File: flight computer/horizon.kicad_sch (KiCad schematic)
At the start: 38 parts, among them J2 Conn_02x03_Counter_Clockwise, J7 Conn_02x03_Counter_Clockwise, J8 Conn_02x03_Counter_Clockwise, SW1 CK_KMS2xxG, U1 MMCU, U2 MKL02Z32VFG4, U3 NMCU, U4 TMCU, Y1 Crystal

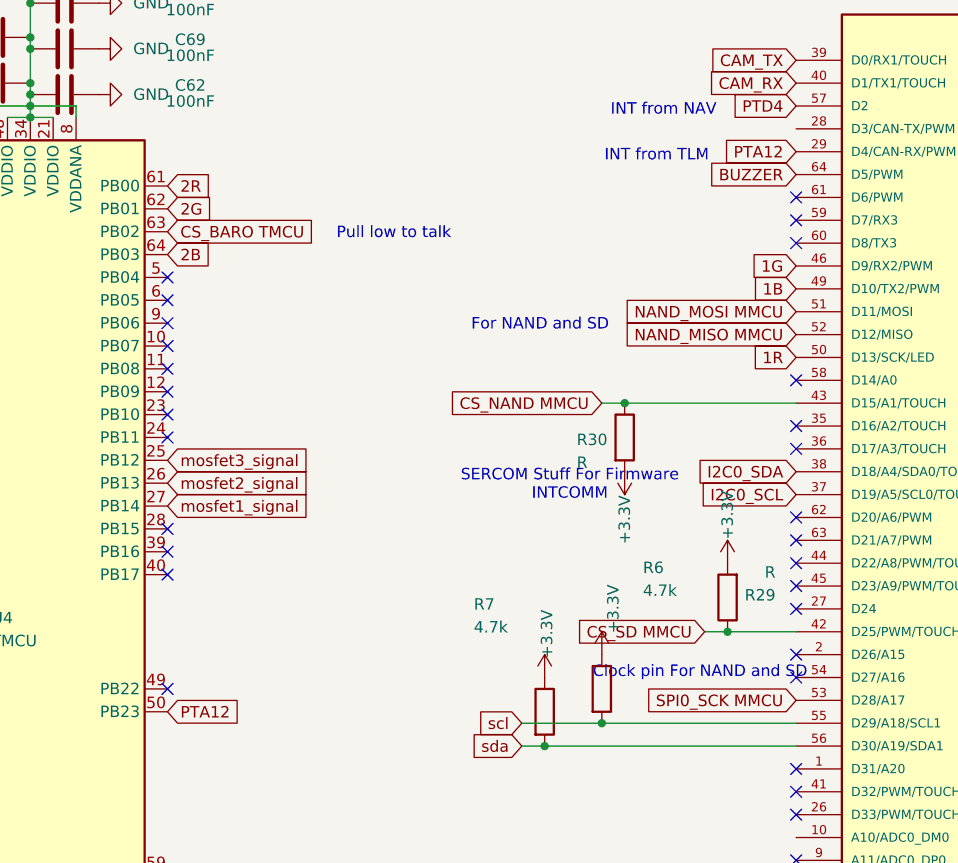
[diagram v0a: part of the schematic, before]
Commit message: one more trace besides for power...
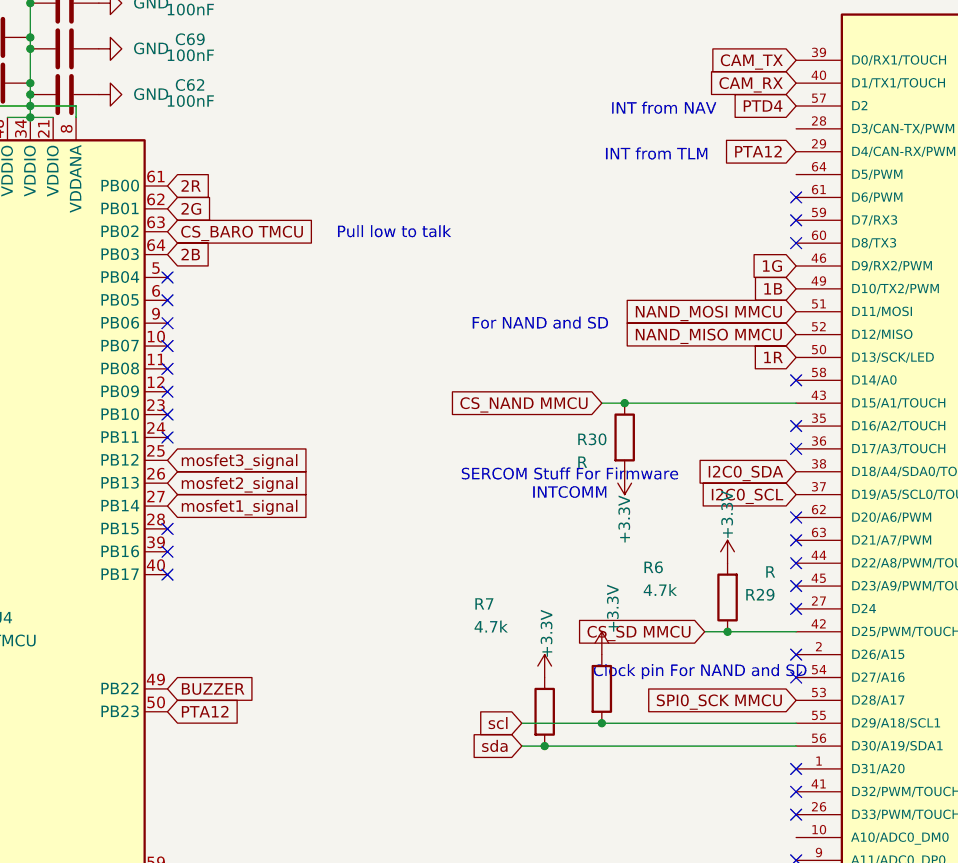
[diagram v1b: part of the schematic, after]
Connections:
- net BUZZER: now also U4.49 (PB22); no longer U1.64 (D5/PWM)
- no-connect marks 73 -> 72

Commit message: status light
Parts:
- added D18: SMLVN6RGB, LED_SMD:LED_ROHM_SMLVN6, symbol LED:SMLVN6RGB
- added R96, R97, R98: 220, Resistor_SMD:R_0603_1608Metric, symbol Device:R
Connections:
- net GND: now also D18.4 (GK), D18.5 (RK), D18.6 (BK)
- net StatusLED_2: now reaches U1.2 (D26/A15)
- net StatusLED_2: now also R97.1
- net StatusLED_1: now reaches U1.27 (D24)
- net StatusLED_1: now also R98.1
- net StatusLED_3: now reaches U1.41 (D32/PWM/TOUCH)
- net StatusLED_3: now also R96.1
- new net: D18.2 (RA), R97.2
- new net: D18.3 (GA), R96.2
- new net: D18.1 (BA), R98.2
- no-connect marks 72 -> 69

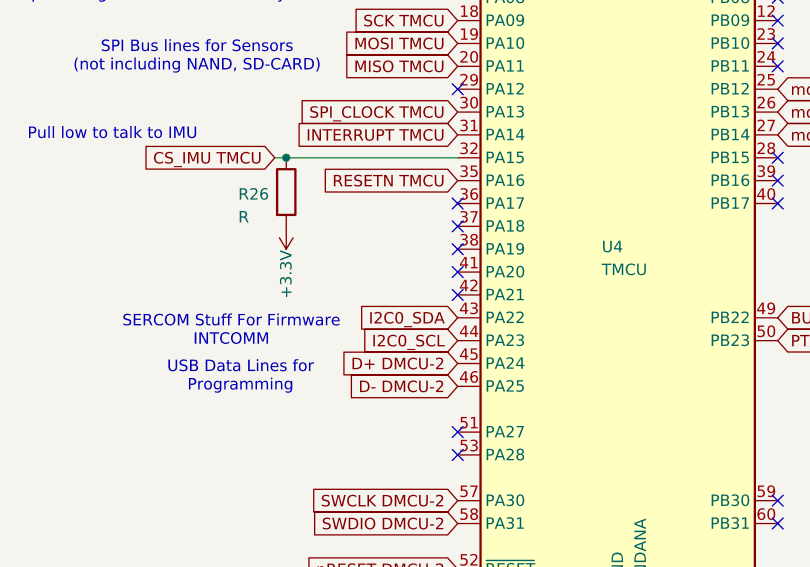
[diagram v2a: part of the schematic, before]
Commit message: Meddy, the PCB is ready for you. The proper RF is setup too on the PCB
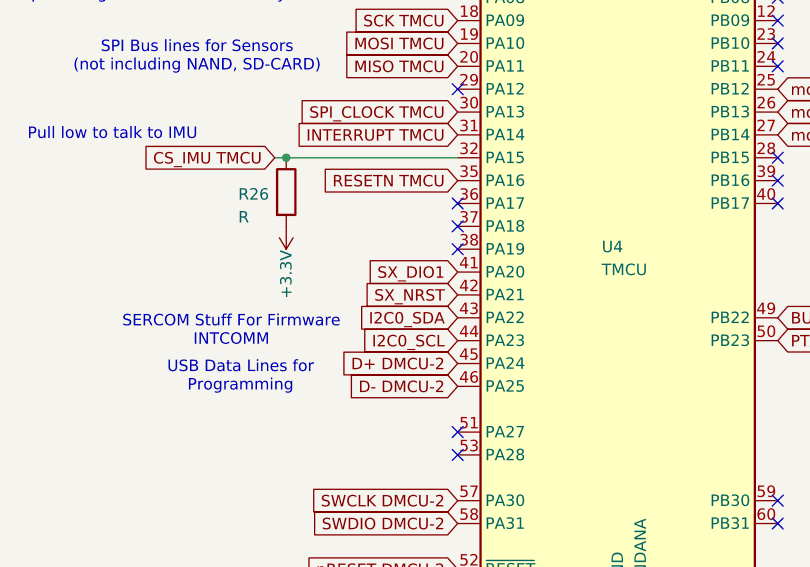
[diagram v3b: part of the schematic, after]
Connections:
- net SX_DIO1: now reaches U4.41 (PA20)
- net SX_NRST: now reaches U4.42 (PA21)
- no-connect marks 69 -> 67
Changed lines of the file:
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@@
-	)
-	(no_connect
-		(at 127 95.25)
 	)
 	(no_connect
@@
 	)
 	(no_connect
-		(at 127 97.79)
-	)
-	(no_connect
 		(at 232.41 99.06)
 	)
@@
 			(effects
 				(font
+					(size 1.27 1.27)
+				)
+				(justify right)
+				(hide yes)
+			)
+		)
+	)
+	(global_label "SX_NRST"
+		(shape input)
+		(at 127 97.79 180)
+		(fields_autoplaced yes)
+		(effects
+			(font
+				(size 1.27 1.27)
+			)
+			(justify right)
+		)
+		(property "Intersheetrefs" "${INTERSHEET_REFS}"
+			(at 115.8506 97.79 0)
+			(effects
+				(font
+					(size 1.27 1.27)
+				)
+				(justify right)
+				(hide yes)
+			)
+		)
+	)
+	(global_label "SX_DIO1"
+		(shape input)
+		(at 127 95.25 180)
+		(fields_autoplaced yes)
+		(effects
+			(font
+				(size 1.27 1.27)
+			)
+			(justify right)
+		)
+		(property "Intersheetrefs" "${INTERSHEET_REFS}"
+			(at 116.2134 95.25 0)
+			(effects
+				(font

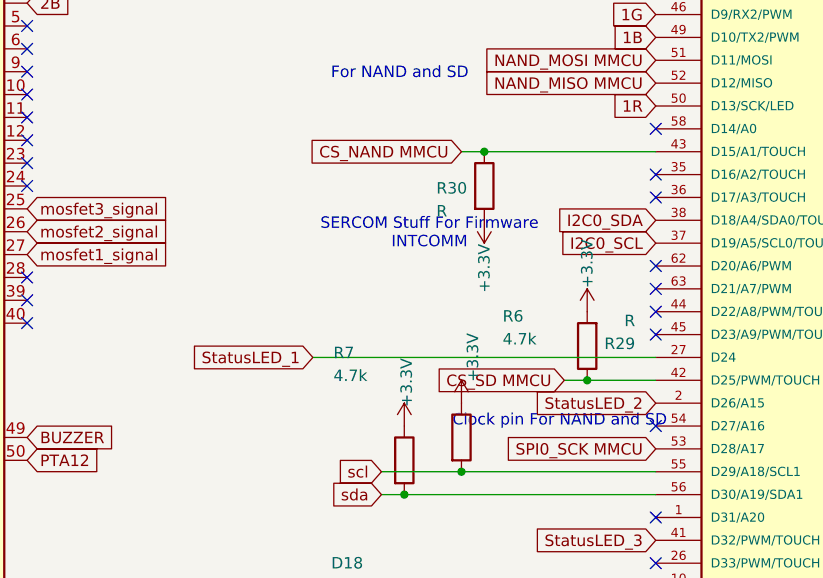
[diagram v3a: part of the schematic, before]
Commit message: js added led
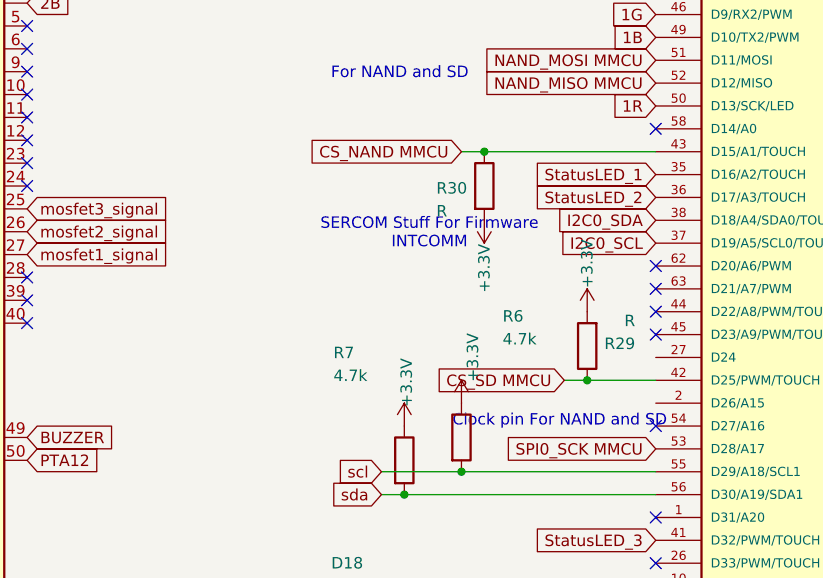
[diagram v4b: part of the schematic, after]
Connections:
- net StatusLED_1: now also U1.35 (D16/A2/TOUCH); no longer U1.27 (D24)
- net StatusLED_2: now also U1.36 (D17/A3/TOUCH); no longer U1.2 (D26/A15)
- no-connect marks 67 -> 65

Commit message: schematic stuff
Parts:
- removed C61, C62, C68, C69, C70, C71, C73, C74, C75, C76: 100nF, Capacitor_SMD:C_0603_1608Metric, symbol Device:C
- added C11, C13, C5, C6, C7, C8, C9: 100nF, Capacitor_SMD:C_0603_1608Metric, symbol Device:C
- added C12: 1uF, Capacitor_SMD:C_0603_1608Metric, symbol Device:C
- added R10, R13: 2.2k, Resistor_SMD:R_0603_1608Metric, symbol Device:R
- added R14, R9: 1.5k, Resistor_SMD:R_0603_1608Metric, symbol Device:R
- R26, R29, R30: value R -> 2.2K
- SAMD21G18A-AU: renamed from U4; footprint Package_QFP:TQFP-64_10x10mm_P0.5mm -> Package_QFP:TQFP-48_7x7mm_P0.5mm; symbol MCU_Microchip_SAMD:ATSAMD21J16B-A -> MCU_Microchip_SAMD:ATSAMD21G18A-A
- SAMD21G18A-AU: renamed from U3; footprint Package_QFP:TQFP-64_10x10mm_P0.5mm -> Package_QFP:TQFP-48_7x7mm_P0.5mm; symbol MCU_Microchip_SAMD:ATSAMD21J16B-A -> MCU_Microchip_SAMD:ATSAMD21G18A-A
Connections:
- net +3.3V: now also SAMD21G18A-AU.17 (VDDIO), SAMD21G18A-AU.17 (VDDIO), SAMD21G18A-AU.36 (VDDIO), SAMD21G18A-AU.36 (VDDIO), SAMD21G18A-AU.44 (VDDIN), SAMD21G18A-AU.44 (VDDIN), SAMD21G18A-AU.6 (VDDANA), SAMD21G18A-AU.6 (VDDANA), C11.2, C13.2, C5.2, C6.2, C7.2, C8.2, C9.2, R10.2, R13.2, R14.2, R9.2; no longer SAMD21G18A-AU.21 (VDDIO), SAMD21G18A-AU.21 (VDDIO), SAMD21G18A-AU.34 (VDDIO), SAMD21G18A-AU.34 (VDDIO), SAMD21G18A-AU.48 (VDDIO), SAMD21G18A-AU.48 (VDDIO), SAMD21G18A-AU.56 (VDDIN), SAMD21G18A-AU.56 (VDDIN), SAMD21G18A-AU.8 (VDDANA), SAMD21G18A-AU.8 (VDDANA)
- net 2B: now also SAMD21G18A-AU.19 (PB10); no longer SAMD21G18A-AU.64 (PB03)
- net 2G: now also SAMD21G18A-AU.8 (PB09); no longer SAMD21G18A-AU.62 (PB01)
- net 2R: now also SAMD21G18A-AU.7 (PB08); no longer SAMD21G18A-AU.61 (PB00)
- net 3B: now also SAMD21G18A-AU.19 (PB10); no longer SAMD21G18A-AU.63 (PB02)
- net 3G: now also SAMD21G18A-AU.8 (PB09); no longer SAMD21G18A-AU.62 (PB01)
- net 3R: now also SAMD21G18A-AU.7 (PB08); no longer SAMD21G18A-AU.61 (PB00)
- net BGM_CS: now also SAMD21G18A-AU.39 (PA27); no longer SAMD21G18A-AU.51 (PA27)
- net BGM_INT: now also SAMD21G18A-AU.41 (PA28); no longer SAMD21G18A-AU.53 (PA28)
- net BGM_RESET: now also SAMD21G18A-AU.15 (PA10); no longer SAMD21G18A-AU.19 (PA10)
- net BUZZER: now also SAMD21G18A-AU.37 (PB22); no longer SAMD21G18A-AU.49 (PB22)
- net CS_BARO TMCU: now also SAMD21G18A-AU.47 (PB02); no longer SAMD21G18A-AU.63 (PB02)
- net CS_IMU TMCU: now also SAMD21G18A-AU.24 (PA15); no longer SAMD21G18A-AU.32 (PA15)
- net D+ DMCU-1: now also SAMD21G18A-AU.33 (PA24), R9.1; no longer SAMD21G18A-AU.45 (PA24)
- net D+ DMCU-2: now also SAMD21G18A-AU.33 (PA24), R14.1; no longer SAMD21G18A-AU.45 (PA24)
- net D- DMCU-1: now also SAMD21G18A-AU.34 (PA25); no longer SAMD21G18A-AU.46 (PA25)
- net D- DMCU-2: now also SAMD21G18A-AU.34 (PA25); no longer SAMD21G18A-AU.46 (PA25)
- net DIR1: now also SAMD21G18A-AU.23 (PA14); no longer SAMD21G18A-AU.31 (PA14)
- net GND: now also SAMD21G18A-AU.18 (GND), SAMD21G18A-AU.18 (GND), SAMD21G18A-AU.35 (GND), SAMD21G18A-AU.35 (GND), SAMD21G18A-AU.42 (GND), SAMD21G18A-AU.42 (GND), C11.1, C12.1, C13.1, C5.1, C6.1, C7.1, C8.1, C9.1; no longer SAMD21G18A-AU.22 (GND), SAMD21G18A-AU.22 (GND), SAMD21G18A-AU.33 (GND), SAMD21G18A-AU.33 (GND), SAMD21G18A-AU.47 (GND), SAMD21G18A-AU.47 (GND), SAMD21G18A-AU.54 (GND), SAMD21G18A-AU.54 (GND)
- net I2C0_SCL: now also SAMD21G18A-AU.32 (PA23), SAMD21G18A-AU.32 (PA23), R10.1; no longer SAMD21G18A-AU.44 (PA23), SAMD21G18A-AU.44 (PA23)
- net I2C0_SDA: now also SAMD21G18A-AU.31 (PA22), SAMD21G18A-AU.31 (PA22), R13.1; no longer SAMD21G18A-AU.43 (PA22), SAMD21G18A-AU.43 (PA22)
- net INTERRUPT TMCU: now also SAMD21G18A-AU.23 (PA14); no longer SAMD21G18A-AU.31 (PA14)
- net MISO TMCU: now also SAMD21G18A-AU.16 (PA11); no longer SAMD21G18A-AU.20 (PA11)
- net MOSI TMCU: now also SAMD21G18A-AU.15 (PA10); no longer SAMD21G18A-AU.19 (PA10)
- net PTA12: now also SAMD21G18A-AU.38 (PB23); no longer SAMD21G18A-AU.50 (PB23)
- net PTD4: now also SAMD21G18A-AU.37 (PB22); no longer SAMD21G18A-AU.49 (PB22)
- net PWM1: now also SAMD21G18A-AU.24 (PA15); no longer SAMD21G18A-AU.32 (PA15)
- net RESETN TMCU: now also SAMD21G18A-AU.25 (PA16); no longer SAMD21G18A-AU.35 (PA16)
- net RF_CS: now also SAMD21G18A-AU.12 (PA07); no longer SAMD21G18A-AU.16 (PA07)
- net RS_GPS TMCU: now also SAMD21G18A-AU.48 (PB03); no longer SAMD21G18A-AU.64 (PB03)
- net RX TMCU: now also SAMD21G18A-AU.10 (PA05); no longer SAMD21G18A-AU.14 (PA05)
- net SCK TMCU: now also SAMD21G18A-AU.14 (PA09); no longer SAMD21G18A-AU.18 (PA09)
- net SERVO5: now also SAMD21G18A-AU.9 (PA04); no longer SAMD21G18A-AU.13 (PA04)
- net SPI_CLOCK TMCU: now also SAMD21G18A-AU.22 (PA13); no longer SAMD21G18A-AU.30 (PA13)
- net SWCLK DMCU-1: now also SAMD21G18A-AU.46 (PA31); no longer SAMD21G18A-AU.58 (PA31)
- net SWCLK DMCU-2: now also SAMD21G18A-AU.45 (PA30); no longer SAMD21G18A-AU.57 (PA30)
- net SWDIO DMCU-1: now also SAMD21G18A-AU.45 (PA30); no longer SAMD21G18A-AU.57 (PA30)
- net SWDIO DMCU-2: now also SAMD21G18A-AU.46 (PA31); no longer SAMD21G18A-AU.58 (PA31)
- net SX_DIO1: now also SAMD21G18A-AU.29 (PA20); no longer SAMD21G18A-AU.41 (PA20)
- net SX_NRST: now also SAMD21G18A-AU.30 (PA21); no longer SAMD21G18A-AU.42 (PA21)
- net TX TMCU: now also SAMD21G18A-AU.9 (PA04); no longer SAMD21G18A-AU.13 (PA04)
- net mosfet1_signal: now also SAMD21G18A-AU.26 (PA17); no longer SAMD21G18A-AU.27 (PB14)
- net mosfet1_signalfire: now also SAMD21G18A-AU.16 (PA11); no longer SAMD21G18A-AU.20 (PA11)
- net mosfet2_signal: now also SAMD21G18A-AU.27 (PA18); no longer SAMD21G18A-AU.26 (PB13)
- net mosfet2_signalfire: now also SAMD21G18A-AU.21 (PA12); no longer SAMD21G18A-AU.29 (PA12)
- net mosfet3_signal: now also SAMD21G18A-AU.28 (PA19); no longer SAMD21G18A-AU.25 (PB12)
- net mosfet4_signal: now also SAMD21G18A-AU.13 (PA08); no longer SAMD21G18A-AU.17 (PA08)
- net mosfet4_signalfire: now also SAMD21G18A-AU.25 (PA16); no longer SAMD21G18A-AU.35 (PA16)
- net mosfet5_signal: now also SAMD21G18A-AU.14 (PA09); no longer SAMD21G18A-AU.18 (PA09)
- net nRESET DMCU-1: now also SAMD21G18A-AU.40 (~{RESET}); no longer SAMD21G18A-AU.52 (~{RESET})
- net nRESET DMCU-2: now also SAMD21G18A-AU.40 (~{RESET}); no longer SAMD21G18A-AU.52 (~{RESET})
- net at C79.2: now also SAMD21G18A-AU.5 (GNDANA); no longer SAMD21G18A-AU.7 (GNDANA)
- net at SAMD21G18A-AU.5 (GNDANA): now also C78.2
- net at C72.2: now also SAMD21G18A-AU.43 (VDDCORE); no longer SAMD21G18A-AU.55 (VDDCORE)
- new net: C12.2, SAMD21G18A-AU.43 (VDDCORE)
- no-connect marks 65 -> 48
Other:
- moved on the sheet: C77

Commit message: finished power stuff
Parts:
- renumbered SAMD21G18A-AU to SAMD21G18A-AU1, SAMD21G18A-AU to SAMD21G18A-AU2
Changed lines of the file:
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@@
 		(on_board yes)
 		(dnp no)
-		(property "Reference" "SAMD21G18A-AU"
+		(property "Reference" "SAMD21G18A-AU2"
 			(at 139.7 87.122 0)
 			(effects
@@
 			(project "horizon"
 				(path "/78d9c2f3-deae-418a-8c21-4820ea8fc57f"
-					(reference "SAMD21G18A-AU")
+					(reference "SAMD21G18A-AU2")
 					(unit 1)
 				)
@@
 		(on_board yes)
 		(dnp no)
-		(property "Reference" "SAMD21G18A-AU"
+		(property "Reference" "SAMD21G18A-AU1"
 			(at 42.926 81.788 0)
 			(effects
@@
 			(project ""
 				(path "/78d9c2f3-deae-418a-8c21-4820ea8fc57f"
-					(reference "SAMD21G18A-AU")
-					(unit 1)
-				)
+					(reference "SAMD21G18A-AU1")
+					(unit 1)
+				)

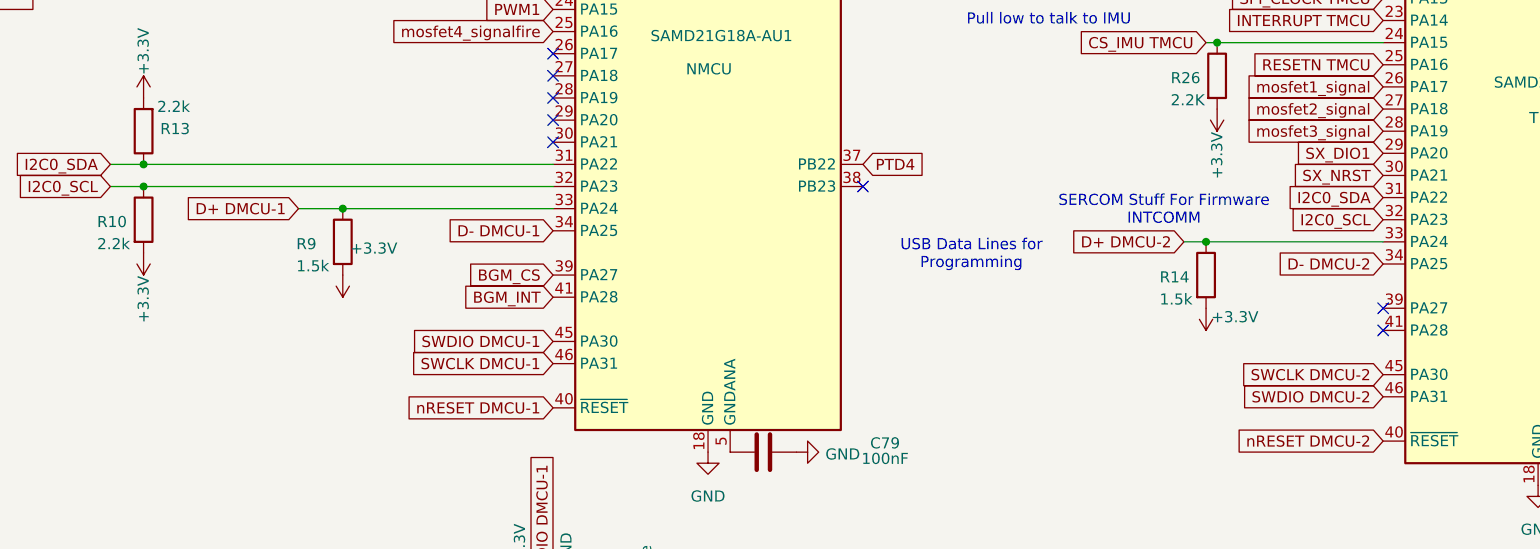
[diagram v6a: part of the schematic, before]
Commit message: data lines fix :(
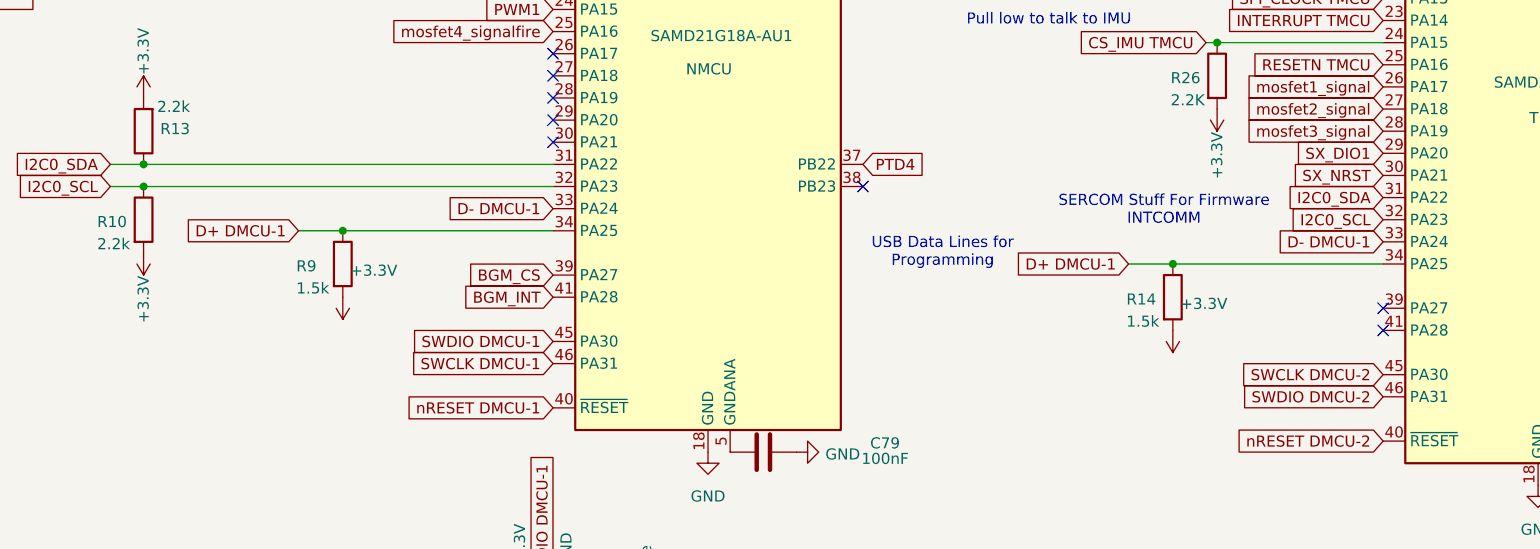
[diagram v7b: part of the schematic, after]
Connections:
- net D- DMCU-2 is gone; now on net D+ DMCU-1: SAMD21G18A-AU2.34 (PA25)
- net D+ DMCU-1: now also R14.1, SAMD21G18A-AU1.34 (PA25); no longer SAMD21G18A-AU1.33 (PA24)
- net D- DMCU-1: now also SAMD21G18A-AU1.33 (PA24), SAMD21G18A-AU2.33 (PA24); no longer SAMD21G18A-AU1.34 (PA25)
- removed net D+ DMCU-2: R14.1, SAMD21G18A-AU2.33 (PA24)
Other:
- moved on the sheet: R9
